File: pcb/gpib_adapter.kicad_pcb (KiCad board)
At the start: 2 copper layers, 73 x 41 mm, 49 parts, among them CON1 AVR-ISP-6, J1 HEADER_2, P2 USB, P3 GPIO, P5 GPIB, U1 SN75160, U2 SN75161, U3 FT230XQ, U4 AT90CAN128-A

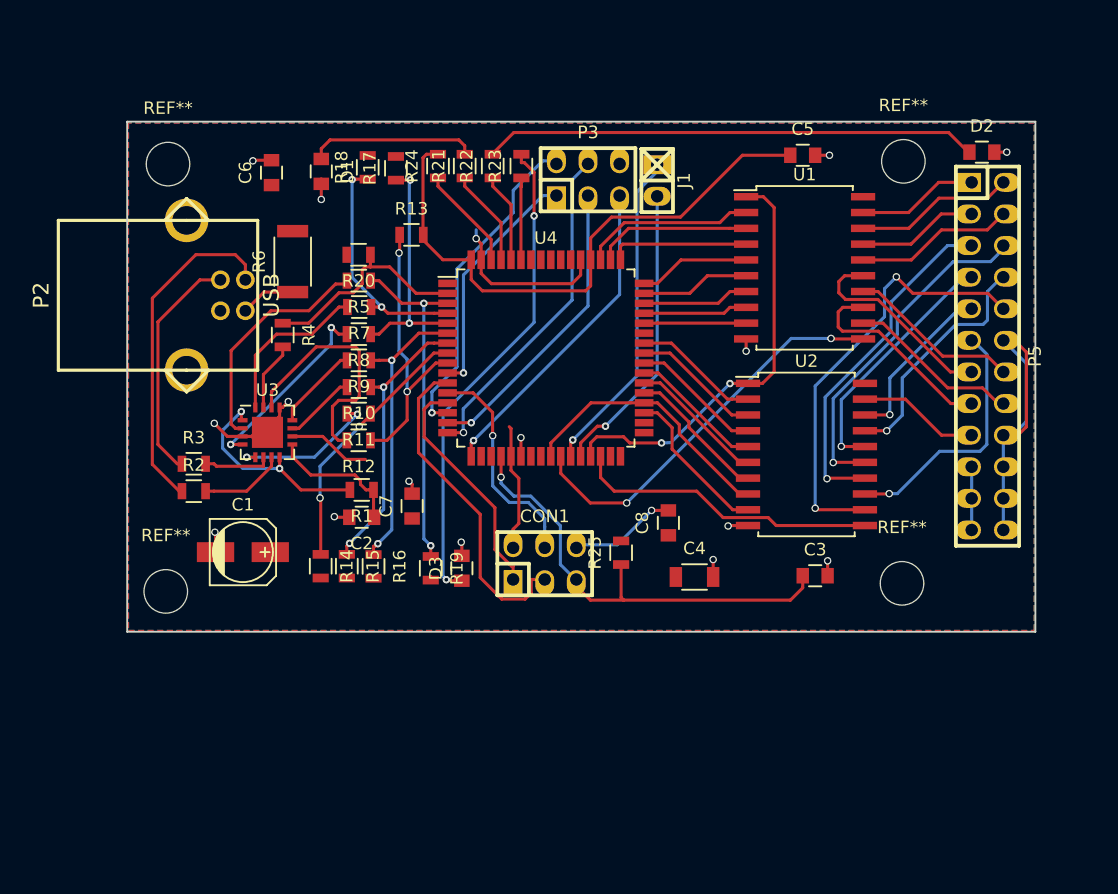
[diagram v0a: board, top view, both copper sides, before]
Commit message: fix: fix gpib adapter connections
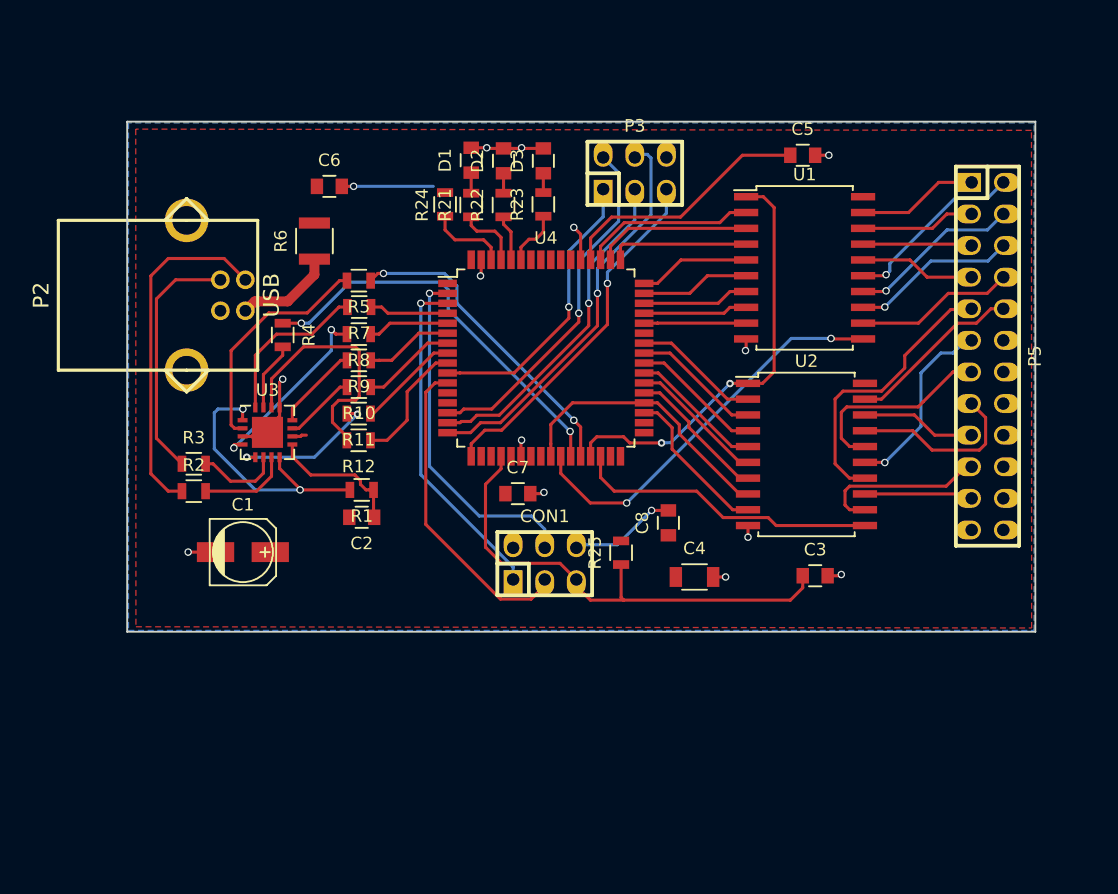
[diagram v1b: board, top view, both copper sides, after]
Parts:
- removed J1: HEADER_2, w_pin_strip:pin_socket_2
- removed R13, R14, R15, R16, R17, R18, R19, R20: R, Resistors_SMD:R_0805
- removed REF** (x4): MountingHole_3-5mm, Mounting_Holes:MountingHole_3-5mm
- R6: footprint Resistors_SMD:R_2010 -> Resistors_SMD:R_1210
- moved D2 38.5 mm to (141.7, 77.3), turned to 90 degrees
- moved D3 33.4 mm to (144.8, 77.3)
- moved D1 12.1 mm to (139.1, 77.3), turned to 90 degrees
- moved C7 8.56 mm to (142.8, 104.1), turned to 0 degrees
- moved C6 4.78 mm to (127.7, 79.4), turned to 0 degrees
- moved P3 3.80 mm to (152.2, 78.3)
- moved R23 3.55 mm to (144.8, 80.8)
- moved R22 3.25 mm to (141.7, 80.9)
- moved R21 3.17 mm to (139.1, 80.9)
- moved R24 3.13 mm to (136.9, 80.8)
- moved R6 2.41 mm to (126.5, 83.8)
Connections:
- net Net-(P2-Pad1) renamed /usbpwr
- net Net-(P2-Pad2) renamed /_usb-
- net Net-(P2-Pad3) renamed /_usb+
- net Net-(R2-Pad2) renamed /usb-
- net Net-(R3-Pad2) renamed /usb+
- P5 pad 10: /SRQ B -> /REN B
- P5 pad 11: /ATN B -> /DAV B
- P5 pad 13: /DIO5 B -> /NRFD B
- P5 pad 14: /DIO6 B -> GND
- P5 pad 15: /DIO7 B -> /NDAC B
- P5 pad 16: /DIO8 B -> GND
- P5 pad 17: /REN B -> /IFC B
- P5 pad 19: GND -> /SRQ B
- P5 pad 2: /DIO2 B -> /DIO5 B
- P5 pad 21: GND -> /ATN B
- P5 pad 3: /DIO3 B -> /DIO2 B
- P5 pad 4: /DIO4 B -> /DIO6 B
- P5 pad 5: /EOI B -> /DIO3 B
- P5 pad 6: /DAV B -> /DIO7 B
- P5 pad 7: /NRFD B -> /DIO4 B
- P5 pad 8: /NDAC B -> /DIO8 B
- P5 pad 9: /IFC B -> /EOI B
- R4 pad 1: Net-(R20-Pad1) -> /RXD
- R5 pad 1: Net-(R19-Pad1) -> /TXD
- U4 pad 12: /MOSI -> (no net)
- U4 pad 13: /MISO -> (no net)
- U4 pad 2: Net-(R20-Pad1) -> /MOSI
- U4 pad 27: /TXD -> /RXD
- U4 pad 28: /RXD -> /TXD
- U4 pad 3: Net-(R19-Pad1) -> /MISO
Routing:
- net +5V: track 65.3 -> 23.2 mm
- net Net-(D2-Pad1): track 39.7 -> 1.60 mm
- net Net-(D3-Pad1): track 39.2 -> 1.55 mm, vias 2 -> 0
- net GND: track 83.7 -> 49.4 mm, vias 17 -> 15
- net Net-(R19-Pad1): track 27.5 -> 0.00 mm, vias 2 -> 0
- net /SRQ B: track 35.5 -> 13.6 mm, vias 2 -> 0
- net Net-(R20-Pad1): track 17.6 -> 0.00 mm
- net Net-(R9-Pad1): track 23.4 -> 7.08 mm, vias 2 -> 0
- net Net-(R10-Pad1): track 22.3 -> 7.64 mm, vias 2 -> 0
- net Net-(R12-Pad1): track 23.6 -> 10.7 mm, vias 2 -> 0
- net Net-(R11-Pad1): track 21.2 -> 8.34 mm, vias 2 -> 0
- net Net-(R8-Pad1): track 19.3 -> 6.55 mm, vias 2 -> 0
- net Net-(R7-Pad1): track 18.9 -> 6.36 mm, vias 2 -> 0
- net /DAV B: track 27.4 -> 15.0 mm
- net /ATN B: track 20.4 -> 8.48 mm, vias 1 -> 0
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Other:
- net class usbpwr added: clearance 0.4, trace_width 0.8, via_dia 0.6, via_drill 0.4
- board text added: "GPIB-USB Converter V1.1 10.10.2015"
- board text removed: "GPIB-USB Converter V1.0 13.09.2015"

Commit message: updating hardware
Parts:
- removed P3: GPIO, w_pin_strip:pin_socket_3x2
- removed R10, R11, R12, R9: R, Resistors_SMD:R_0805
- added C9: 22µ, Capacitors_SMD:c_elec_5x5.3, F.Cu at (131.2, 80.8)
- added J1: HEADER_5x2, w_pin_strip:pin_strip_5x2, F.Cu at (149.2, 78.7)
- added REF**: MountingHole_3-5mm, Mounting_Holes:MountingHole_3-5mm, F.Cu at (115.8, 78.8)
- added REF**: MountingHole_3-5mm, Mounting_Holes:MountingHole_3-5mm, F.Cu at (115.6, 111.3)
- added REF**: MountingHole_3-5mm, Mounting_Holes:MountingHole_3-5mm, F.Cu at (180.2, 112.2)
- C4: footprint Capacitors_SMD:C_1206 -> Capacitors_SMD:C_0805
- moved D1 35.3 mm to (147.4, 111.6), turned to 270 degrees
- moved D3 34.5 mm to (140.2, 111.5), turned to 270 degrees
- moved D2 34.2 mm to (144.0, 111.4), turned to 270 degrees
- moved C8 29.2 mm to (136.9, 83.4)
- moved R21 28.4 mm to (147.4, 108.0), turned to 270 degrees
- moved R23 27.5 mm to (140.2, 108.0), turned to 270 degrees
- moved R22 27.1 mm to (144.0, 107.9), turned to 270 degrees
- moved C6 23.2 mm to (133.8, 101.8), turned to 270 degrees
- moved CON1 21.3 mm to (132.8, 92.3), turned to 270 degrees
- moved C1 12.8 mm to (133.4, 110.3)
- moved R5 11.9 mm to (126.8, 98.5)
- moved C3 10.4 mm to (156.3, 111.7)
- moved R4 9.80 mm to (126.8, 100.7), turned to 180 degrees
- moved C4 9.15 mm to (166.1, 110.0)
- moved R1 7.89 mm to (125.2, 109.9)
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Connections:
- R21 pad 1: Net-(R21-Pad1) -> /TALK
- R22 pad 1: Net-(R22-Pad1) -> /MODE
- R23 pad 1: Net-(R23-Pad1) -> /PWR
- U1 pad 12: /DIO8 B -> /DIO1
- U1 pad 13: /DIO7 B -> /DIO2
- U1 pad 14: /DIO6 B -> /DIO3
- U1 pad 15: /DIO5 B -> /DIO4
- U1 pad 16: /DIO4 B -> /DIO5
- U1 pad 17: /DIO3 B -> /DIO6
- U1 pad 18: /DIO2 B -> /DIO7
- U1 pad 19: /DIO1 B -> /DIO8
- U1 pad 2: /DIO1 -> /DIO8 B
- U1 pad 3: /DIO2 -> /DIO7 B
- U1 pad 4: /DIO3 -> /DIO6 B
- U1 pad 5: /DIO4 -> /DIO5 B
- U1 pad 6: /DIO5 -> /DIO4 B
- U1 pad 7: /DIO6 -> /DIO3 B
- U1 pad 8: /DIO7 -> /DIO2 B
- U1 pad 9: /DIO8 -> /DIO1 B
- U2 pad 12: /SRQ B -> /SRQ
- U2 pad 13: /ATN B -> /ATN
- U2 pad 14: /EOI B -> /EOI
- U2 pad 15: /DAV B -> /DAV
- U2 pad 16: /NRFD B -> /NRFD
- U2 pad 17: /NDAC B -> /NDAC
- U2 pad 18: /IFC B -> /IFC
- U2 pad 19: /REN B -> /REN
- U2 pad 2: /REN -> /REN B
- U2 pad 3: /IFC -> /IFC B
- U2 pad 4: /NDAC -> /NDAC B
- U2 pad 5: /NRFD -> /NRFD B
- U2 pad 6: /DAV -> /DAV B
- U2 pad 7: /EOI -> /EOI B
- U2 pad 8: /ATN -> /ATN B
- U2 pad 9: /SRQ -> /SRQ B
- U3 pad 11: Net-(R10-Pad2) -> (no net)
- U3 pad 12: Net-(R9-Pad2) -> (no net)
- U3 pad 14: Net-(R12-Pad2) -> (no net)
- U3 pad 5: Net-(R11-Pad2) -> (no net)
- U4 pad 10: /GPIO1 -> (no net)
- U4 pad 14: /GPIO2 -> (no net)
- U4 pad 15: /GPIO3 -> /PWR
- U4 pad 16: /GPIO4 -> /MODE
- U4 pad 17: /GPIO5 -> /TALK
- U4 pad 35: /SRQ -> /REN
- U4 pad 36: /ATN -> /IFC
- U4 pad 37: /EOI -> /NDAC
- U4 pad 38: /DAV -> /NRFD
- U4 pad 39: /NRFD -> /DAV
- U4 pad 40: /NDAC -> /EOI
- U4 pad 41: /IFC -> /ATN
- U4 pad 42: /REN -> /SRQ
- U4 pad 54: (no net) -> /TDI
- U4 pad 55: (no net) -> /TDO
- U4 pad 56: (no net) -> /TMS
- U4 pad 57: (no net) -> /TCK
- U4 pad 59: Net-(R23-Pad1) -> (no net)
- U4 pad 6: Net-(R9-Pad1) -> (no net)
- U4 pad 60: Net-(R22-Pad1) -> (no net)
- U4 pad 61: Net-(R21-Pad1) -> (no net)
- U4 pad 7: Net-(R10-Pad1) -> (no net)
- U4 pad 8: Net-(R11-Pad1) -> (no net)
- U4 pad 9: Net-(R12-Pad1) -> (no net)
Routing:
- net /GPIO4: track 32.3 -> 0.00 mm, vias 1 -> 0
- net /GPIO2: track 28.9 -> 0.00 mm, vias 1 -> 0
- net /GPIO5: track 28.5 -> 0.00 mm, vias 1 -> 0
- net /GPIO3: track 26.8 -> 0.00 mm, vias 1 -> 0
- net /GPIO1: track 22.8 -> 0.00 mm, vias 1 -> 0
- net /RESET: track 40.0 -> 60.5 mm, vias 0 -> 4
- net Net-(R12-Pad2): track 19.9 -> 0.00 mm
- net /MOSI: track 28.0 -> 8.19 mm, vias 1 -> 0
- net /MISO: track 27.9 -> 8.55 mm
- net /SCK: track 25.4 -> 8.93 mm
- net GND: track 49.4 -> 34.1 mm, vias 15 -> 16
- net Net-(R11-Pad2): track 11.9 -> 0.00 mm, vias 2 -> 0
- net /PWR: track 0.00 -> 11.0 mm
- net /TALK: track 0.00 -> 10.9 mm
- net /EOI B: track 23.7 -> 12.9 mm
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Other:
- board text added: "GPIB-USB Converter V1.1 14.10.2015"
- board text removed: "GPIB-USB Converter V1.1 10.10.2015"

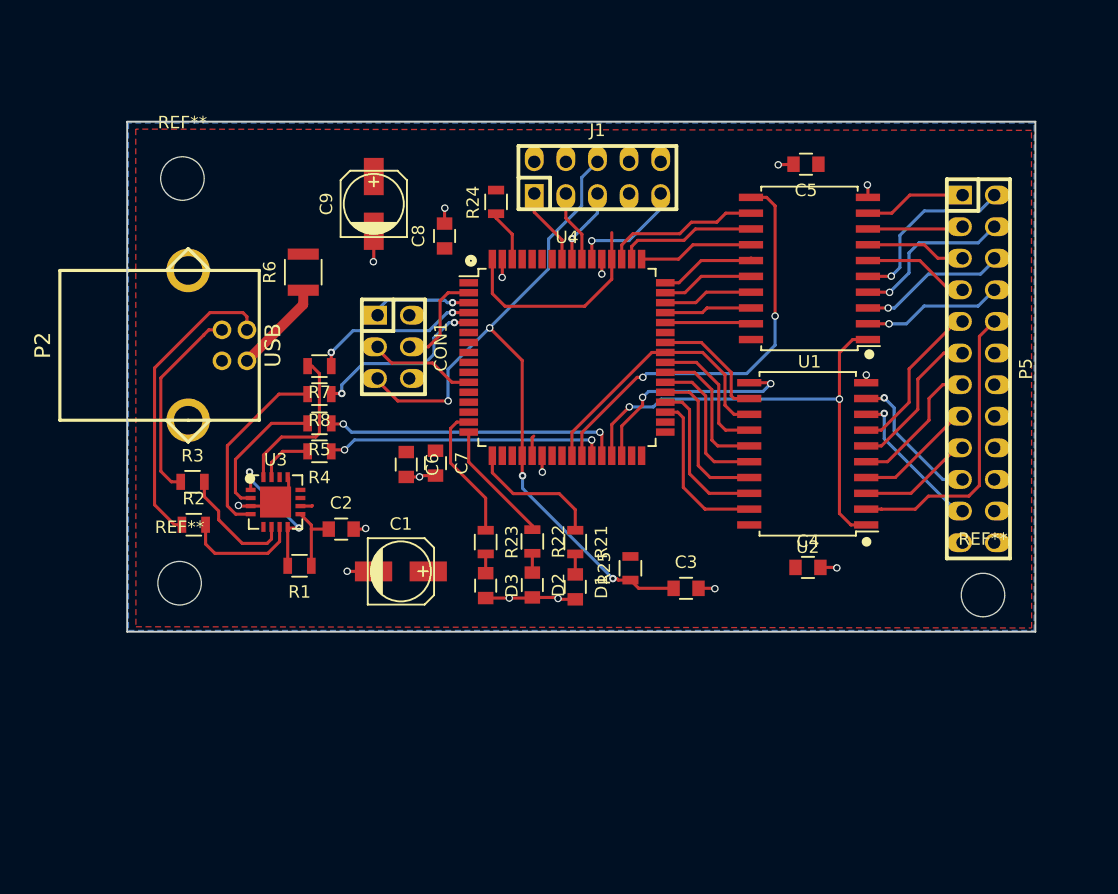
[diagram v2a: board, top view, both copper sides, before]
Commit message: add enclosure drawing
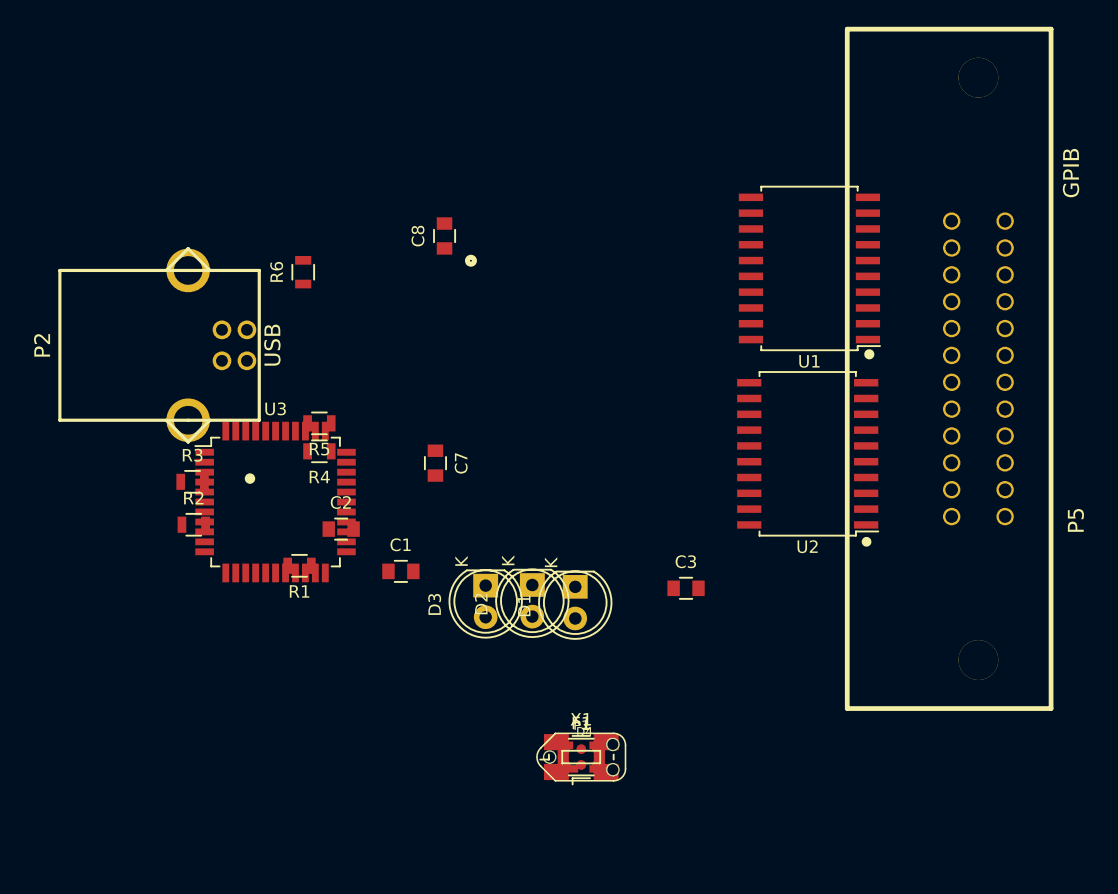
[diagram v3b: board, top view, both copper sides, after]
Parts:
- removed C4: 1µ, Capacitors_SMD:C_0805
- removed C5, C6: 100n, Capacitors_SMD:C_0805
- removed C9: 22µ, Capacitors_SMD:c_elec_5x5.3
- removed CON1: AVR-ISP-6, w_pin_strip:pin_socket_3x2
- removed J1: HEADER_5x2, w_pin_strip:pin_strip_5x2
- removed R21, R22, R23, R24, R25, R7, R8: R, Resistors_SMD:R_0805
- removed REF** (x3): MountingHole_3-5mm, Mounting_Holes:MountingHole_3-5mm
- removed U4: AT90CAN128-A, Housings_QFP:LQFP-64_14x14mm_Pitch0.8mm
- added D4: PRTR5V0U2X, esd_protection:PRTR5V0U2X, F.Cu at (147.9, 125.3)
- added F1: F_Small, Resistors_SMD:R_1210, F.Cu at (147.9, 125.3)
- added P1: TC2030-MCP, tagconnect:TC2030-NL_SMALL, F.Cu at (147.9, 125.3)
- added X1: 8MHz, Crystals:Crystal_SMD_5032_4Pads, F.Cu at (147.9, 125.3)
- C1: value 22µ -> 1u; footprint Capacitors_SMD:c_elec_5x5.3 -> Capacitors_SMD:C_0805
- C2, C3: value 100n -> 18p
- D1, D2, D3: footprint Capacitors_SMD:C_0805 -> LEDs:LED-5MM
- P5: footprint w_pin_strip:pin_socket_12x2 -> gpib_conn_male:gpib_conn_male
- R4, R5: value R -> 470
- R6: value R -> 470; footprint Resistors_SMD:R_1210 -> Resistors_SMD:R_0805
- U3: value FT230XQ -> PIC18(L)F4550-I/PT; footprint Housings_DFN_QFN:QFN-16-1EP_4x4mm_Pitch0.65mm -> Housings_QFP:TQFP-44_10x10mm_Pitch0.8mm
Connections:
- C1 pad 1: +5V -> /VUSB
- C2 pad 1: Net-(C2-Pad1) -> /OSCI
- C3 pad 1: /RESET -> /OSCO
- R1 pad 1: Net-(C2-Pad1) -> +5V
- R1 pad 2: Net-(R1-Pad2) -> /MCLR
- R4 pad 1: /RXD -> Net-(D1-Pad1)
- R4 pad 2: Net-(R4-Pad2) -> /TALK
- R5 pad 1: /TXD -> Net-(D2-Pad1)
- R5 pad 2: Net-(R5-Pad2) -> /MODE
- R6 pad 1: /usbpwr -> Net-(D3-Pad1)
- R6 pad 2: +5V -> /PWR
- U3 pad 1: Net-(R1-Pad2) -> /ATN
- U3 pad 10: +5V -> /TXD
- U3 pad 11: (no net) -> /TE
- U3 pad 12: (no net) -> Net-(U3-Pad12)
- U3 pad 13: GND -> Net-(U3-Pad13)
- U3 pad 14: (no net) -> /DC
- U3 pad 15: Net-(R4-Pad2) -> Net-(U3-Pad15)
- U3 pad 16: Net-(R7-Pad2) -> /PGC
- U3 pad 17: GND -> /PGD
- U3 pad 2: Net-(R5-Pad2) -> /DIO5
- U3 pad 3: GND -> /DIO6
- U3 pad 4: Net-(R8-Pad2) -> /DIO7
- U3 pad 5: (no net) -> /DIO8
- U3 pad 6: /usb+ -> GND
- U3 pad 7: /usb- -> +5V
- U3 pad 8: Net-(R1-Pad2) -> /PE
- U3 pad 9: Net-(C2-Pad1) -> /RXD
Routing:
- net /RESET: track 60.5 -> 0.00 mm, vias 4 -> 0
- net /TE: track 39.8 -> 0.00 mm, vias 2 -> 0
- net GND: track 34.1 -> 0.00 mm, vias 16 -> 0
- net /PE: track 33.7 -> 0.00 mm, vias 2 -> 0
- net /_usb-: track 24.9 -> 0.00 mm
- net /REN B: track 23.9 -> 0.00 mm
- net /TXD: track 23.8 -> 0.00 mm, vias 2 -> 0
- net /RXD: track 22.6 -> 0.00 mm, vias 2 -> 0
- net /ATN: track 22.3 -> 0.00 mm
- net +5V: track 20.3 -> 0.00 mm
- net /DC: track 17.9 -> 0.00 mm, vias 2 -> 0
- net /_usb+: track 16.0 -> 0.00 mm
- net Net-(R8-Pad2): track 15.2 -> 0.00 mm
- net /DIO5 B: track 14.7 -> 0.00 mm, vias 1 -> 0
- net Net-(R8-Pad1): track 14.6 -> 0.00 mm, vias 2 -> 0
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- removed copper zone on F.Cu, net +5V
- removed copper zone on B.Cu, net GND
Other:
- board outline removed
- board text added: "Enclosure Digikey HM355-ND"
- board text removed: "GPIB-USB Converter V1.1 14.10.2015"
